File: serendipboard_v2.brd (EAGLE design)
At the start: 34.3 x 48.3 mm, 85 parts, among them IC1 TP4056, IC2 DW01A, IC3 DS3231/SO, J4 USB3076-XX-X_REVC, Q1 FS8205A, Q2 MMBT2222ALT1G, Q3 RUC002N05HZGT116, Q4 DMG3415U, Q5 MMBT2222ALT1G, Q7 RUC002N05HZGT116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

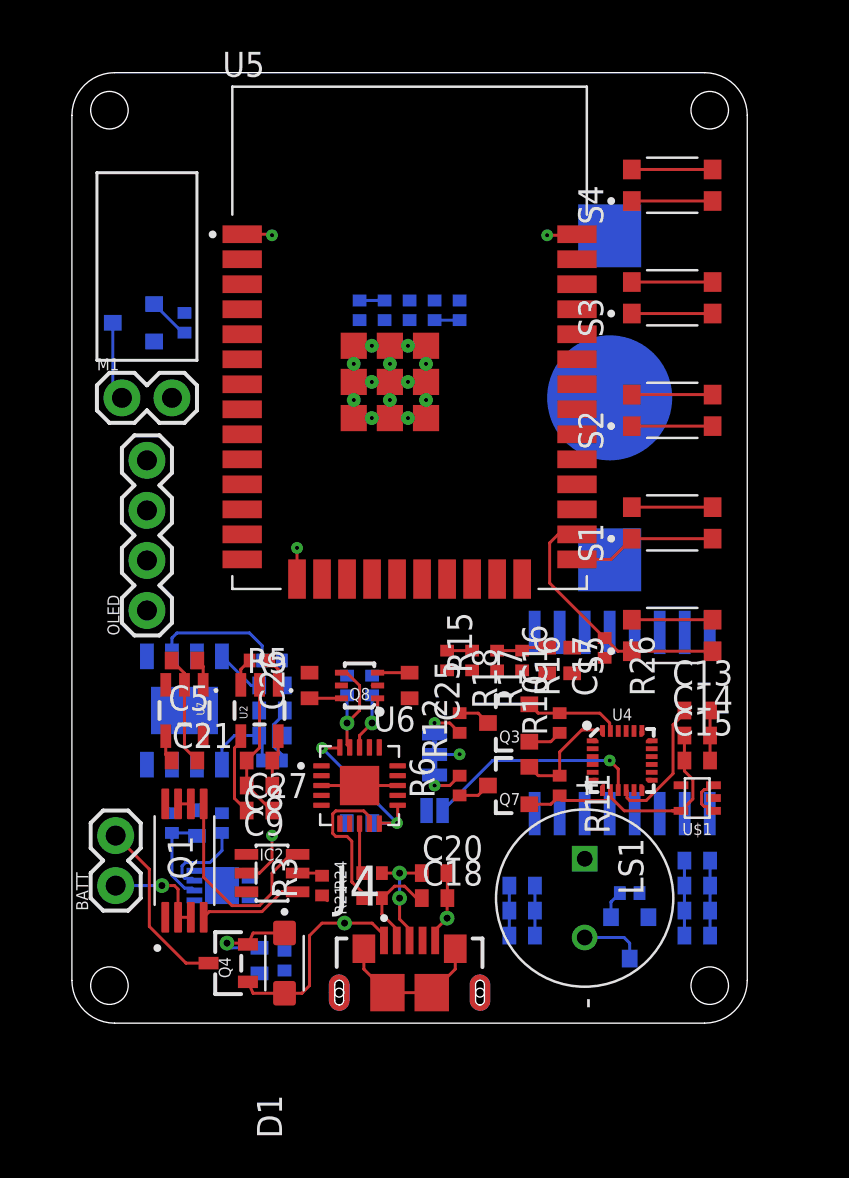
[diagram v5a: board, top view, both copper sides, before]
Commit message: Update serendipboard_v2.brd
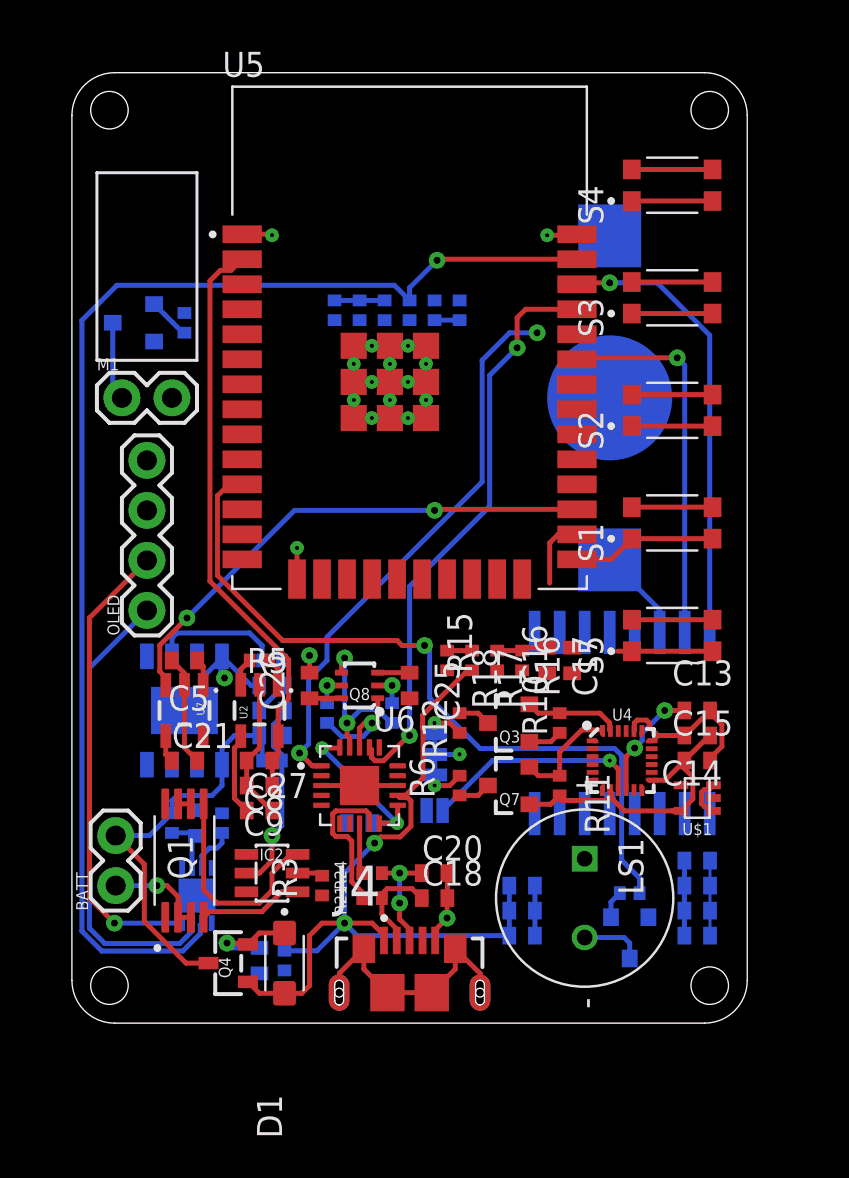
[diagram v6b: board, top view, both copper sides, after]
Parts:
- moved R26 20.5 mm to (15.9, 36.2), flipped to the bottom, turned to 90 degrees
- moved R22 2.68 mm to (13.0, 15.7)
- moved R23 2.68 mm to (16.3, 15.7)
- moved U1 1.37 mm to (6.35, 6.48), turned to 270 degrees
- moved R27 1.27 mm to (14.6, 36.2)
- moved R28 1.27 mm to (13.3, 36.2)
- turned C14 to 180 degrees
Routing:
- net QST: track 0.00 -> 65.8 mm, vias 0 -> 1
- net SCL: track 1.65 -> 48.2 mm, vias 0 -> 1
- net SDA: track 1.65 -> 44.5 mm, vias 0 -> 2
- net BUZZER: track 0.00 -> 38.6 mm, vias 0 -> 1
- net VBUS: track 16.0 -> 47.5 mm, vias 1 -> 3
- net TXD: track 0.00 -> 29.8 mm, vias 0 -> 2
- net RXD: track 0.00 -> 28.5 mm, vias 0 -> 2
- net 3.3V_ESP: track 3.90 -> 32.3 mm
- net LOAD_EN: track 0.00 -> 26.2 mm, vias 0 -> 2
- net GND: track 57.0 -> 65.5 mm, vias 4 -> 5
- net VBAT: track 13.4 -> 21.3 mm
- net PWR: track 13.3 -> 8.42 mm
- net N$9: track 0.00 -> 4.74 mm
- net SHIELD: track 7.70 -> 11.7 mm
- net N$3: track 5.79 -> 9.81 mm
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
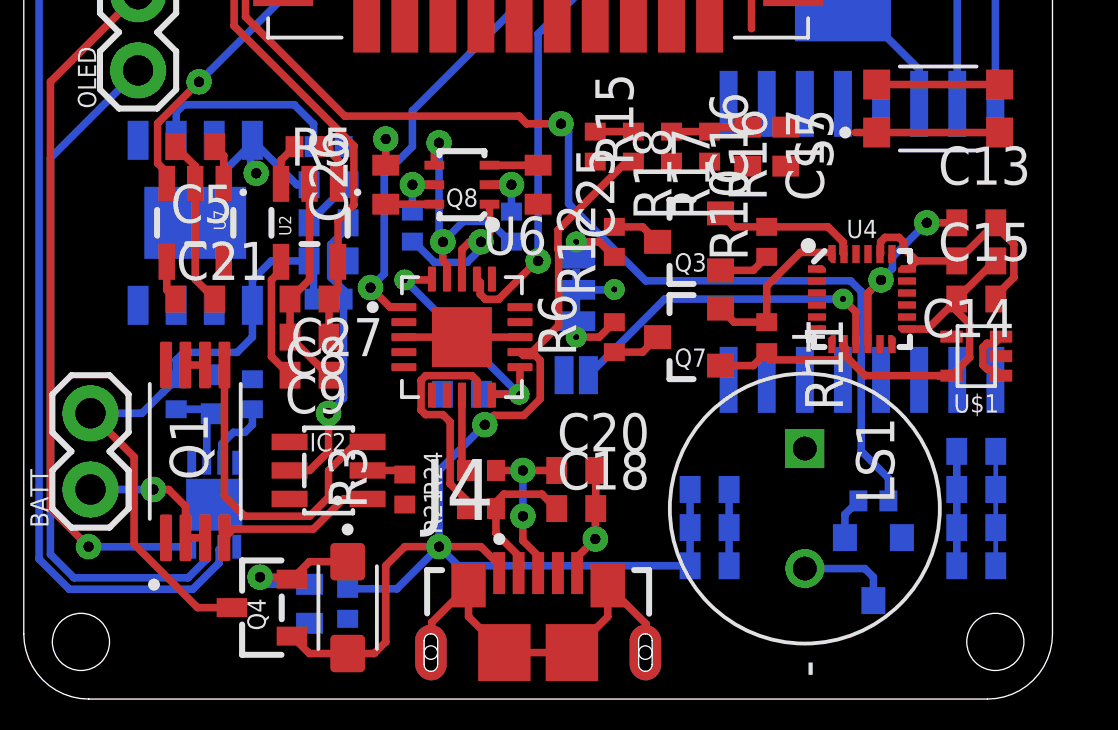
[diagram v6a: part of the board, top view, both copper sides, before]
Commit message: Update serendipboard_v2.brd
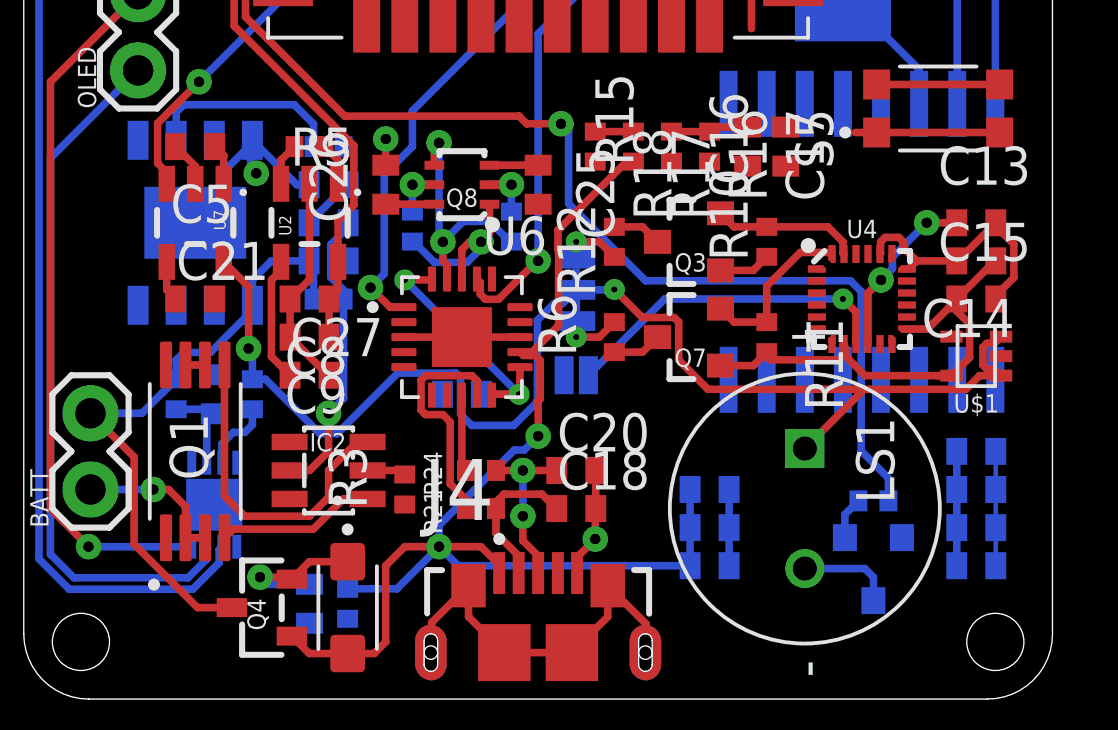
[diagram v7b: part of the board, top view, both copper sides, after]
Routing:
- net VCC: track 8.45 -> 48.0 mm, vias 1 -> 2
- net GND: track 65.5 -> 61.4 mm
- net VBAT: track 21.3 -> 20.8 mm
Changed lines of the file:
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@@
 <wire x1="5.065" y1="18.415" x2="5.715" y2="17.765" width="0.254" layer="1"/>
 <wire x1="5.715" y1="17.765" x2="5.715" y2="17.1751" width="0.254" layer="1"/>
-<wire x1="6.365" y1="13.335" x2="5.715" y2="13.985" width="0.254" layer="1"/>
-<wire x1="5.715" y1="13.985" x2="5.715" y2="17.1751" width="0.254" layer="1"/>
 <wire x1="8.875" y1="13.335" x2="8.875" y2="12.065" width="0.254" layer="1"/>
 <wire x1="8.875" y1="12.065" x2="10.145" y2="10.795" width="0.254" layer="1"/>
@@
 <wire x1="10.81" y1="14.605" x2="9.51" y2="15.875" width="0" layer="19" extent="16-16"/>
 <wire x1="6.365" y1="13.335" x2="8.875" y2="13.335" width="0" layer="19" extent="1-1"/>
-<wire x1="6.35" y1="18.625" x2="5.095" y2="18.415" width="0" layer="19" extent="1-16"/>
-<wire x1="3.81" y1="18.625" x2="5.065" y2="18.415" width="0" layer="19" extent="1-16"/>
 <wire x1="6.04" y1="11.135" x2="6.365" y2="13.335" width="0" layer="19" extent="1-1"/>
 <wire x1="6.35" y1="10.81" x2="6.04" y2="11.135" width="0" layer="19" extent="1-16"/>
@@
 <wire x1="8.86" y1="6.67" x2="7.1" y2="7.877" width="0" layer="19" extent="1-16"/>
 <wire x1="19.065" y1="7.62" x2="18.0086" y2="10.795" width="0" layer="19" extent="1-16"/>
+<wire x1="6.35" y1="18.625" x2="9.525" y2="17.1751" width="0" layer="19" extent="1-16"/>
+<wire x1="5.095" y1="18.415" x2="6.35" y2="18.625" width="0" layer="19" extent="1-16"/>
+<wire x1="3.81" y1="18.625" x2="5.065" y2="18.415" width="0" layer="19" extent="1-16"/>
 <wire x1="12.7" y1="6.485" x2="8.86" y2="6.67" width="0" layer="19" extent="1-1"/>
 <wire x1="11.43" y1="22.548" x2="12.065" y2="18.669" width="0" layer="19" extent="1-1"/>
@@
 <wire x1="19.6723" y1="13.6398" x2="18.415" y2="13.6398" width="0.254" layer="16"/>
 <wire x1="19.685" y1="35.695" x2="18.415" y2="35.695" width="0.254" layer="16"/>
+<wire x1="31.8592125" y1="10.78" x2="32.575" y2="10.78" width="0.254" layer="1"/>
+<wire x1="31.4052125" y1="10.326" x2="31.8592125" y2="10.78" width="0.254" layer="1"/>
+<wire x1="26.035" y1="8.35" x2="28.011" y2="10.326" width="0.254" layer="1"/>
+<wire x1="31.4052125" y1="10.326" x2="28.011" y2="10.326" width="0.254" layer="1"/>
+<wire x1="21.829" y1="12.5702125" x2="21.6802125" y2="12.719" width="0.254" layer="1"/>
+<wire x1="21.6802125" y1="12.719" x2="20.6185" y2="12.719" width="0.254" layer="1"/>
+<wire x1="20.6185" y1="12.719" x2="19.685" y2="13.6525" width="0.254" layer="1"/>
+<wire x1="28.011" y1="10.326" x2="22.8047875" y2="10.326" width="0.254" layer="1"/>
+<wire x1="22.8047875" y1="10.326" x2="21.829" y2="11.3017875" width="0.254" layer="1"/>
+<wire x1="21.829" y1="11.3017875" x2="21.829" y2="12.5702125" width="0.254" layer="1"/>
+<wire x1="6.665" y1="14.5749" x2="7.493" y2="13.7469" width="0.254" layer="1"/>
+<wire x1="7.493" y1="13.7469" x2="7.493" y2="11.684" width="0.254" layer="1"/>
+<via x="7.493" y="11.684" extent="1-16" drill="0.35"/>
+<wire x1="7.493" y1="11.684" x2="7.62" y2="11.557" width="0.254" layer="16"/>
+<wire x1="7.62" y1="11.557" x2="7.62" y2="10.66" width="0.254" layer="16"/>
+<wire x1="18.415" y1="13.6398" x2="17.9578" y2="13.1826" width="0.254" layer="16"/>
+<wire x1="17.9578" y1="13.1826" x2="17.6747875" y2="13.1826" width="0.254" layer="16"/>
+<wire x1="14.559" y1="10.7152125" x2="14.4102125" y2="10.864" width="0.254" layer="16"/>
+<wire x1="10.4429125" y1="8.842" x2="9.8770875" y2="8.842" width="0.254" layer="16"/>
+<wire x1="17.6747875" y1="13.1826" x2="17.118" y2="12.6258125" width="0.254" layer="16"/>
+<wire x1="17.118" y1="9.90815625" x2="17.118" y2="12.6258125" width="0.254" layer="16"/>
+<wire x1="14.4102125" y1="10.864" x2="12.4649125" y2="10.864" width="0.254" layer="16"/>
+<wire x1="12.4649125" y1="10.864" x2="10.4429125" y2="8.842" width="0.254" layer="16"/>
+<wire x1="14.559" y1="9.4940875" x2="14.932965625" y2="9.120121875" width="0.254" layer="16"/>
+<wire x1="14.559" y1="9.4940875" x2="14.559" y2="10.7152125" width="0.254" layer="16"/>
+<wire x1="8.0590875" y1="10.66" x2="7.62" y2="10.66" width="0.254" layer="16"/>
+<wire x1="9.8770875" y1="8.842" x2="8.0590875" y2="10.66" width="0.254" layer="16"/>
+<wire x1="14.932965625" y1="9.120121875" x2="16.329965625" y2="9.120121875" width="0.254" layer="16"/>
+<wire x1="16.329965625" y1="9.120121875" x2="17.118" y2="9.90815625" width="0.254" layer="16"/>
 <wire x1="5.08" y1="31.75" x2="18.415" y2="35.695" width="0" layer="19" extent="16-16"/>
 <wire x1="3.81" y1="28.575" x2="5.08" y2="31.75" width="0" layer="19" extent="1-1"/>
 <wire x1="6.665" y1="14.5749" x2="3.81" y2="28.575" width="0" layer="19" extent="1-1"/>
-<wire x1="7.62" y1="10.66" x2="6.665" y2="14.5749" width="0" layer="19" extent="1-16"/>
-<wire x1="18.415" y1="13.6398" x2="7.62" y2="10.66" width="0" layer="19" extent="16-16"/>
-<wire x1="26.035" y1="8.35" x2="19.685" y2="13.6525" width="0" layer="19" extent="1-1"/>
-<wire x1="31.1" y1="8.255" x2="26.035" y2="8.35" width="0" layer="19" extent="16-16"/>
-<wire x1="31.115" y1="10.64" x2="31.1" y2="8.255" width="0" layer="19" extent="16-16"/>
-<wire x1="32.575" y1="10.78" x2="31.115" y2="10.64" width="0" layer="19" extent="1-16"/>
+<wire x1="26.035" y1="8.35" x2="32.575" y2="10.78" width="0" layer="19" extent="1-16"/>
+<wire x1="31.1" y1="8.255" x2="31.115" y2="10.64" width="0" layer="19" extent="16-16"/>
 </signal>
 <signal name="CHARGER_EN">
@@
 <wire x1="9.5175" y1="1.518" x2="10.795" y2="1.518" width="0.254" layer="1"/>
 <wire x1="17.0454375" y1="11.454" x2="17.214" y2="11.2854375" width="0.254" layer="1"/>
-<wire x1="15.679" y1="9.456" x2="15.367" y2="9.144" width="0.254" layer="1"/>
+<wire x1="17.145" y1="8.763" x2="17.145" y2="9.93515625" width="0.254" layer="1"/>
+<wire x1="17.214" y1="10.00415625" x2="17.145" y2="9.93515625" width="0.254" layer="1"/>
 <wire x1="16.54" y1="11.565" x2="16.651" y2="11.454" width="0.254" layer="1"/>
 <wire x1="16.651" y1="11.454" x2="16.891" y2="11.454" width="0.254" layer="1"/>
 <wire x1="16.891" y1="11.454" x2="17.0454375" y2="11.454" width="0.254" layer="1"/>
 <wire x1="17.214" y1="11.2854375" x2="17.214" y2="10.00415625" width="0.254" layer="1"/>
-<wire x1="17.214" y1="10.00415625" x2="16.66584375" y2="9.456" width="0.254" layer="1"/>
-<wire x1="16.66584375" y1="9.456" x2="15.679" y2="9.456" width="0.254" layer="1"/>
-<via x="15.367" y="9.144" extent="1-16" drill="0.35"/>
-<wire x1="13.843" y1="5.08" x2="13.843" y2="7.62" width="0.254" layer="16"/>
-<wire x1="13.843" y1="7.62" x2="15.367" y2="9.144" width="0.254" layer="16"/>
+<via x="17.145" y="8.763" extent="1-16" drill="0.35"/>
 <wire x1="7.62" y1="18.625" x2="7.62" y2="18.5357875" width="0.254" layer="16"/>
 <wire x1="7.62" y1="18.5357875" x2="7.55960625" y2="18.47539375" width="0.254" layer="16"/>
@@
 <wire x1="7.747" y1="17.526" x2="7.55960625" y2="17.71339375" width="0.254" layer="16"/>
 <wire x1="7.55960625" y1="17.71339375" x2="7.55960625" y2="18.47539375" width="0.254" layer="16"/>
+<wire x1="16.3540875" y1="8.303" x2="16.685" y2="8.303" width="0.254" layer="16"/>
+<wire x1="16.685" y1="8.303" x2="17.145" y2="8.763" width="0.254" layer="16"/>
+<wire x1="13.843" y1="5.08" x2="13.843" y2="5.7919125" width="0.254" layer="16"/>
+<wire x1="13.843" y1="5.7919125" x2="16.3540875" y2="8.303" width="0.254" layer="16"/>
 <wire x1="16.54" y1="11.565" x2="9.51" y2="17.145" width="0" layer="19" extent="1-16"/>
 </signal>
@@
 <wire x1="5.08" y1="10.66" x2="5.08" y2="11.303" width="0.254" layer="16"/>
 <wire x1="5.08" y1="11.303" x2="5.334" y2="11.557" width="0.254" layer="16"/>
-<wire x1="5.334" y1="11.557" x2="7.112" y2="11.557" width="0.254" layer="16"/>
-<wire x1="7.112" y1="11.557" x2="7.62" y2="12.065" width="0.254" layer="16"/>
-<wire x1="7.62" y1="12.065" x2="7.62" y2="13.125" width="0.254" layer="16"/>
+<wire x1="5.334" y1="11.557" x2="6.223" y2="11.557" width="0.254" layer="16"/>
+<wire x1="6.223" y1="11.557" x2="7.62" y2="12.954" width="0.254" layer="16"/>
+<wire x1="7.62" y1="12.954" x2="7.62" y2="13.125" width="0.254" layer="16"/>
 <wire x1="5.08" y1="10.66" x2="4.634" y2="10.214" width="0.254" layer="16"/>
 <wire x1="4.634" y1="10.214" x2="4.6247875" y2="10.214" width="0.254" layer="16"/>

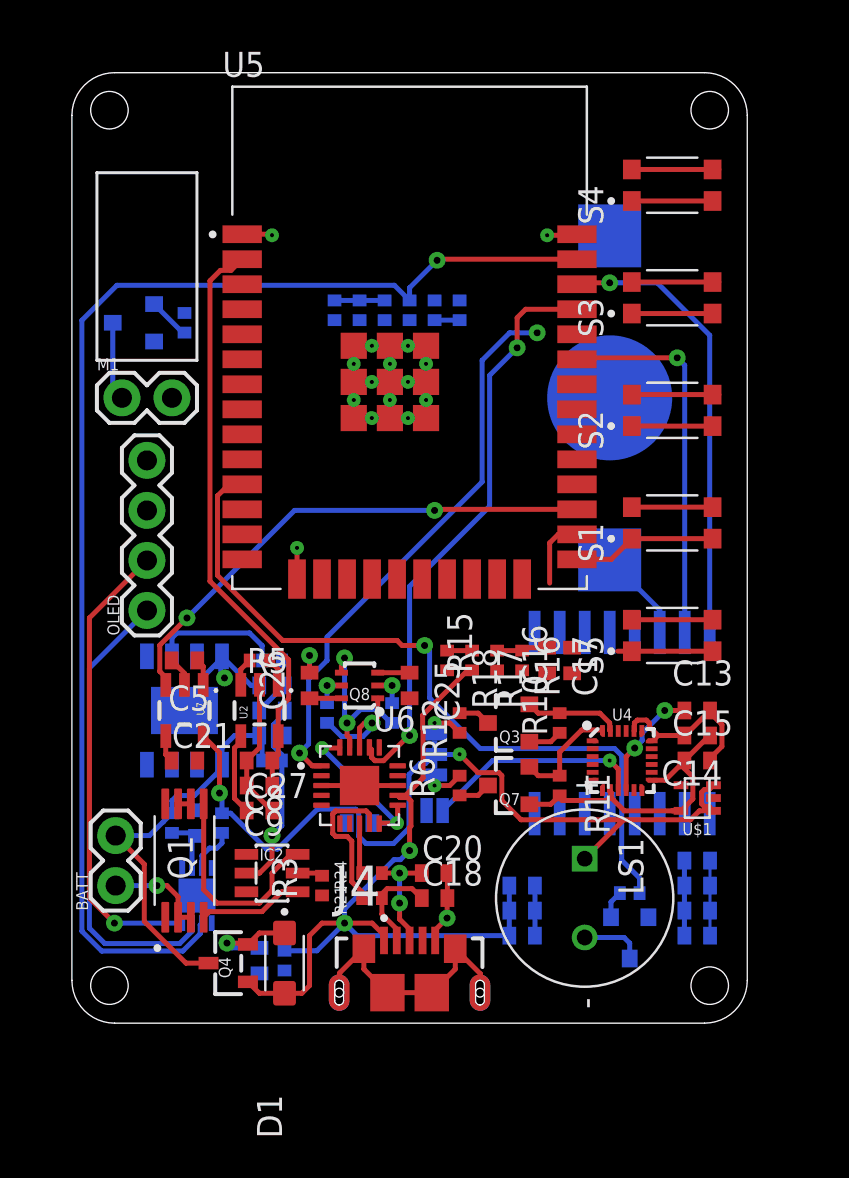
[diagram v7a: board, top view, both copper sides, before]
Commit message: Update serendipboard_v2.brd
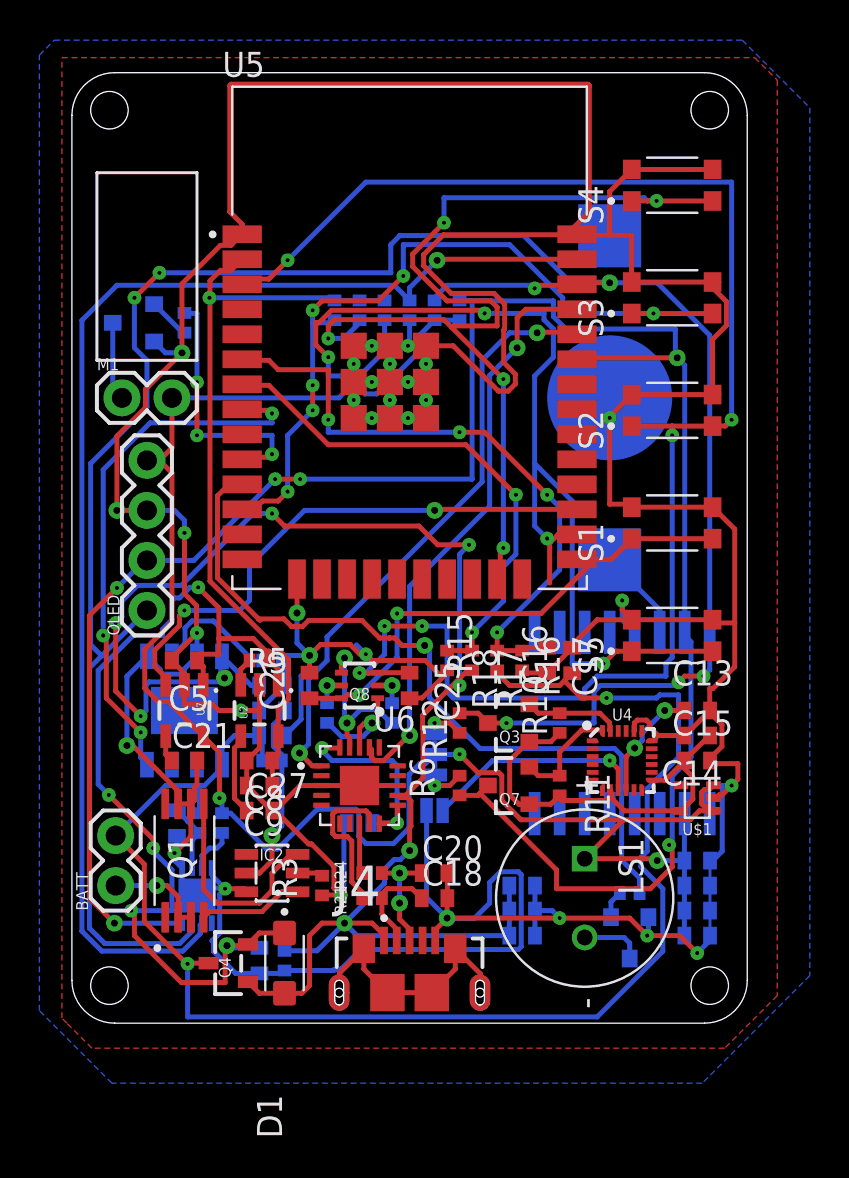
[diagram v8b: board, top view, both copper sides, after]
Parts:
- moved R8 1.40 mm to (6.48, 10.2)
- moved C6 1.02 mm to (5.33, 10.2), turned to 270 degrees
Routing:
- net GND: track 61.4 -> 340.3 mm, vias 5 -> 19
- net EN: track 5.72 -> 81.3 mm, vias 0 -> 6
- net SCL: track 48.2 -> 118.5 mm, vias 1 -> 7
- net SDA: track 44.5 -> 110.8 mm, vias 2 -> 6
- net VBAT: track 20.8 -> 75.2 mm, vias 0 -> 2
- net GPIO15: track 4.10 -> 50.9 mm, vias 0 -> 5
- net PWR: track 8.42 -> 54.4 mm, vias 0 -> 4
- net VCC: track 48.0 -> 91.7 mm, vias 2 -> 3
- net VIN: track 7.85 -> 49.0 mm, vias 1 -> 5
- net VBUS: track 47.1 -> 86.0 mm, vias 3 -> 8
- net GPIO27: track 4.10 -> 39.3 mm, vias 0 -> 6
- net BATT_MONITOR: track 2.60 -> 32.3 mm, vias 0 -> 4
- net CHARGER_EN: track 0.10 -> 27.7 mm, vias 0 -> 3
- net CHARGER: track 1.27 -> 26.3 mm, vias 0 -> 2
- net IO0: track 8.94 -> 26.8 mm, vias 0 -> 2
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- added copper zone on layer 16, net GND
- added copper zone on layer 1, net VCC
